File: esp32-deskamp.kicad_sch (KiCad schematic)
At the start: 3 parts, among them K1 TQ2-12V, U1 ESP32 D1 Mini, U2 TSR 1-2433

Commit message: Rebuild chunk of schematic
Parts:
- added D1, D2, D3, D4: 1N4004, Diode_THT:D_DO-41_SOD81_P10.16mm_Horizontal, symbol Diode:1N4004
- added J1: INPUT 00, symbol Connector:Conn_01x04_Pin
- added J10: SLEEP, symbol Connector:Conn_01x02_Pin
- added J2: INPUT 01, symbol Connector:Conn_01x04_Pin
- added J3: PRE OUT, symbol Connector:Conn_01x04_Pin
- added J4: LFE OUT, symbol Connector:Conn_01x02_Pin
- added J5: 12V IN, symbol Connector:Conn_01x02_Pin
- added J6, J7: JUMPER, symbol Connector:Conn_01x03_Pin
- added J8: INPUT SELECT, symbol Connector:Conn_01x04_Pin
- added J9: MUTE, symbol Connector:Conn_01x02_Pin
- added K2: INPUT 01, RELAY_TQ2_PAN, symbol panasonic-tq2:TQ2-12V
- added K3: AMP MUTE, RELAY_TQ2_PAN, symbol panasonic-tq2:TQ2-12V
- added K4: AMP SLEEP, RELAY_TQ2_PAN, symbol panasonic-tq2:TQ2-12V
- added Q1, Q2, Q3, Q4: 2N3904, Package_TO_SOT_THT:TO-92_Inline, symbol Transistor_BJT:2N3904
- added R1, R2, R5, R6: 1K6, symbol Device:R
- added R3, R4, R7, R8, R9: 10K, symbol Device:R
- added RV1: RK27112MC, Potentiometer_THT:Potentiometer_Alps_RK27112MC, symbol custom:RK27112MC
- added U3: L9110, symbol L9110:L9110
- K1: value TQ2-12V -> INPUT 00
- U1: value ESP32 D1 Mini -> ESP32 D1 MINI
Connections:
- net +12V: now also K1.1, D1.1 (K), D2.1 (K), D3.1 (K), D4.1 (K), J5.1 (Pin_1), K2.1, K3.1, K4.1
- net +3V3: now also U1.16 (3V3), R7.1, R8.1, R9.1
- net at K1.10: now also D1.2 (A), Q1.3 (C)
- net at K1.3: now also J1.1 (Pin_1)
- net PRE_RIGHT: now reaches K1.4
- net PRE_RIGHT: now also K2.4, RV1.4
- net PRE_LEFT: now reaches K1.7
- net PRE_LEFT: now also K2.7, RV1.1
- net at K1.8: now also J1.2 (Pin_2)
- net GNDD renamed GNDS
- net GNDS: now also J5.2 (Pin_2), J8.1 (Pin_1), Q1.1 (E), Q2.1 (E), Q3.1 (E), Q4.1 (E)
- new net: Q1.2 (B), R1.1
- new net: Q4.2 (B), R6.1
- new net: D4.2 (A), K4.10, Q4.3 (C)
- new net: D3.2 (A), K3.10, Q3.3 (C)
- new net: J6.3 (Pin_3), J9.1 (Pin_1)
- new net: J6.2 (Pin_2), J9.2 (Pin_2), K3.4
- new net: J2.1 (Pin_1), K2.3
- new net: J2.2 (Pin_2), K2.8
- new net: D2.2 (A), K2.10, Q2.3 (C)
- new net: Q3.2 (B), R5.1
- new net: J10.1 (Pin_1), J7.3 (Pin_3)
- new net: J10.2 (Pin_2), J7.2 (Pin_2), K4.4
- new net: J4.2 (Pin_2), R3.1, R4.1
- new net: J3.3 (Pin_3), R3.2, RV1.5
- new net: J3.4 (Pin_4), R4.2, RV1.2
- new net: Q2.2 (B), R2.1
- new net: J7.1 (Pin_1), K4.3
- new net: J6.1 (Pin_1), K3.3
- new net GNDA: J1.3 (Pin_3), J1.4 (Pin_4), J2.3 (Pin_3), J2.4 (Pin_4), J3.1 (Pin_1), J3.2 (Pin_2), J4.1 (Pin_1), RV1.3, RV1.6
- new net Input0: R1.2
- new net Input1: R2.2
- new net Mute: R5.2
- new net Select0: J8.4 (Pin_4), R9.2
- new net Select1: J8.3 (Pin_3), R8.2
- new net Select3: J8.2 (Pin_2), R7.2
- new net Sleep: R6.2
- no-connect marks 0 -> 20
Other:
- note added: "INPUT SELECT"
- note added: "OUTPUT STAGE"
- note added: "POWER"
- note added: "TA2024 USES SWITCH LOGIC TO ACTIVATE MUTE/SLEEP. JUMPER 1/2 FOR DIRECT, 2/3 VIA JST."
- moved on the sheet: K1, U1, U2

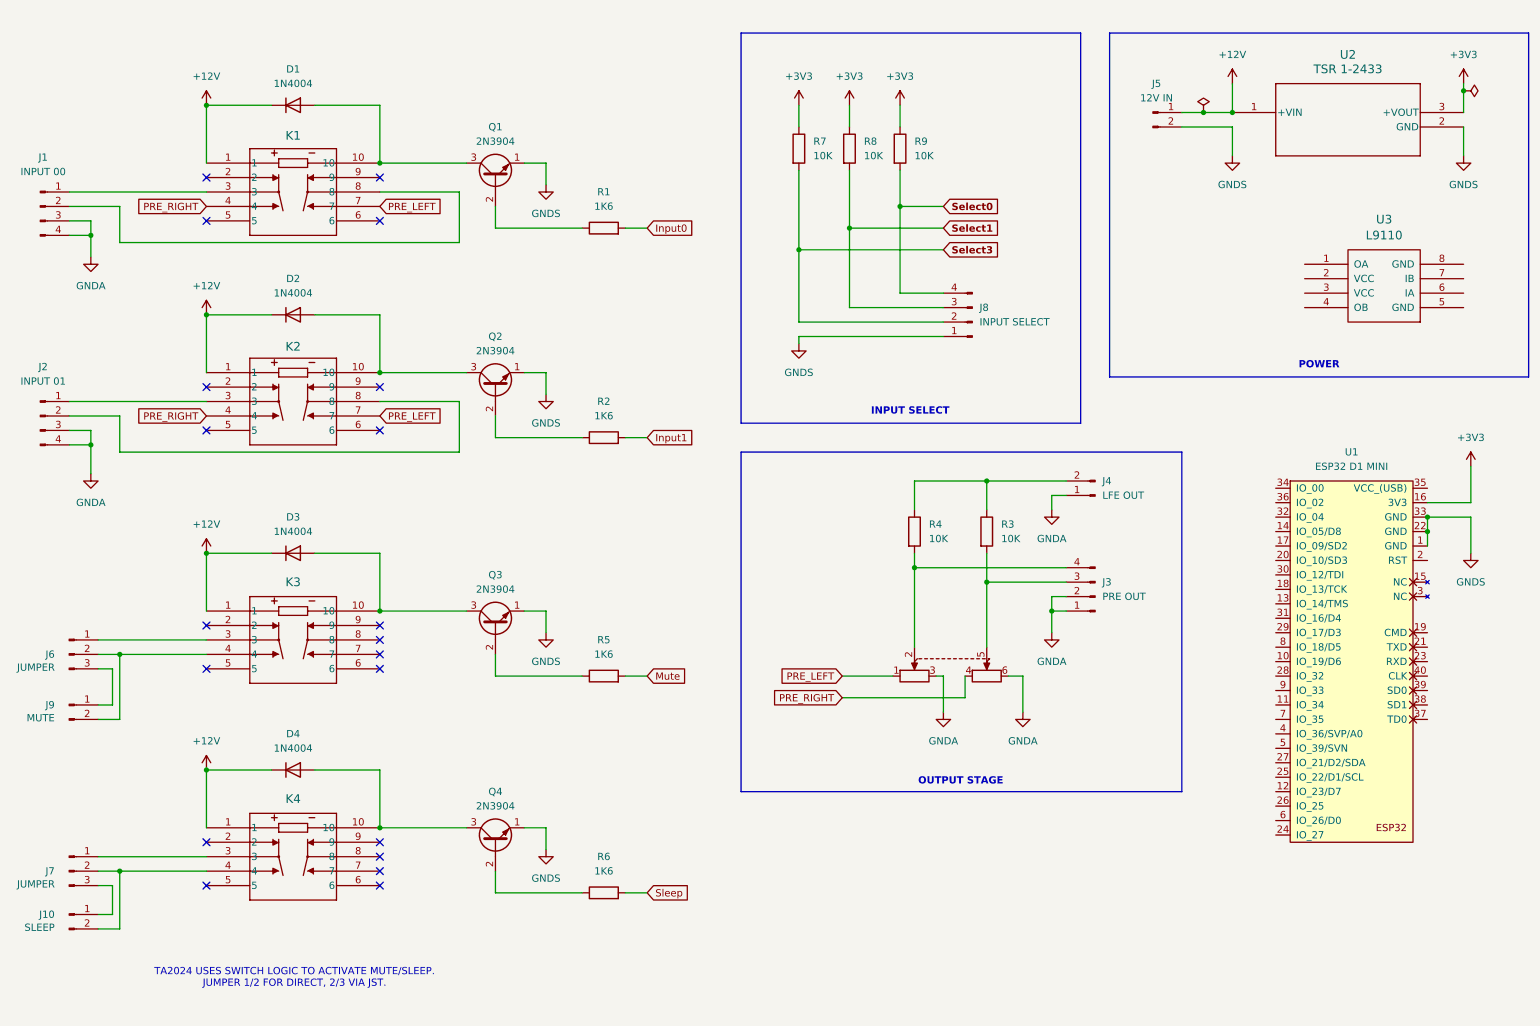
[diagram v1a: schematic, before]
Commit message: Start routing, remove duplicate project
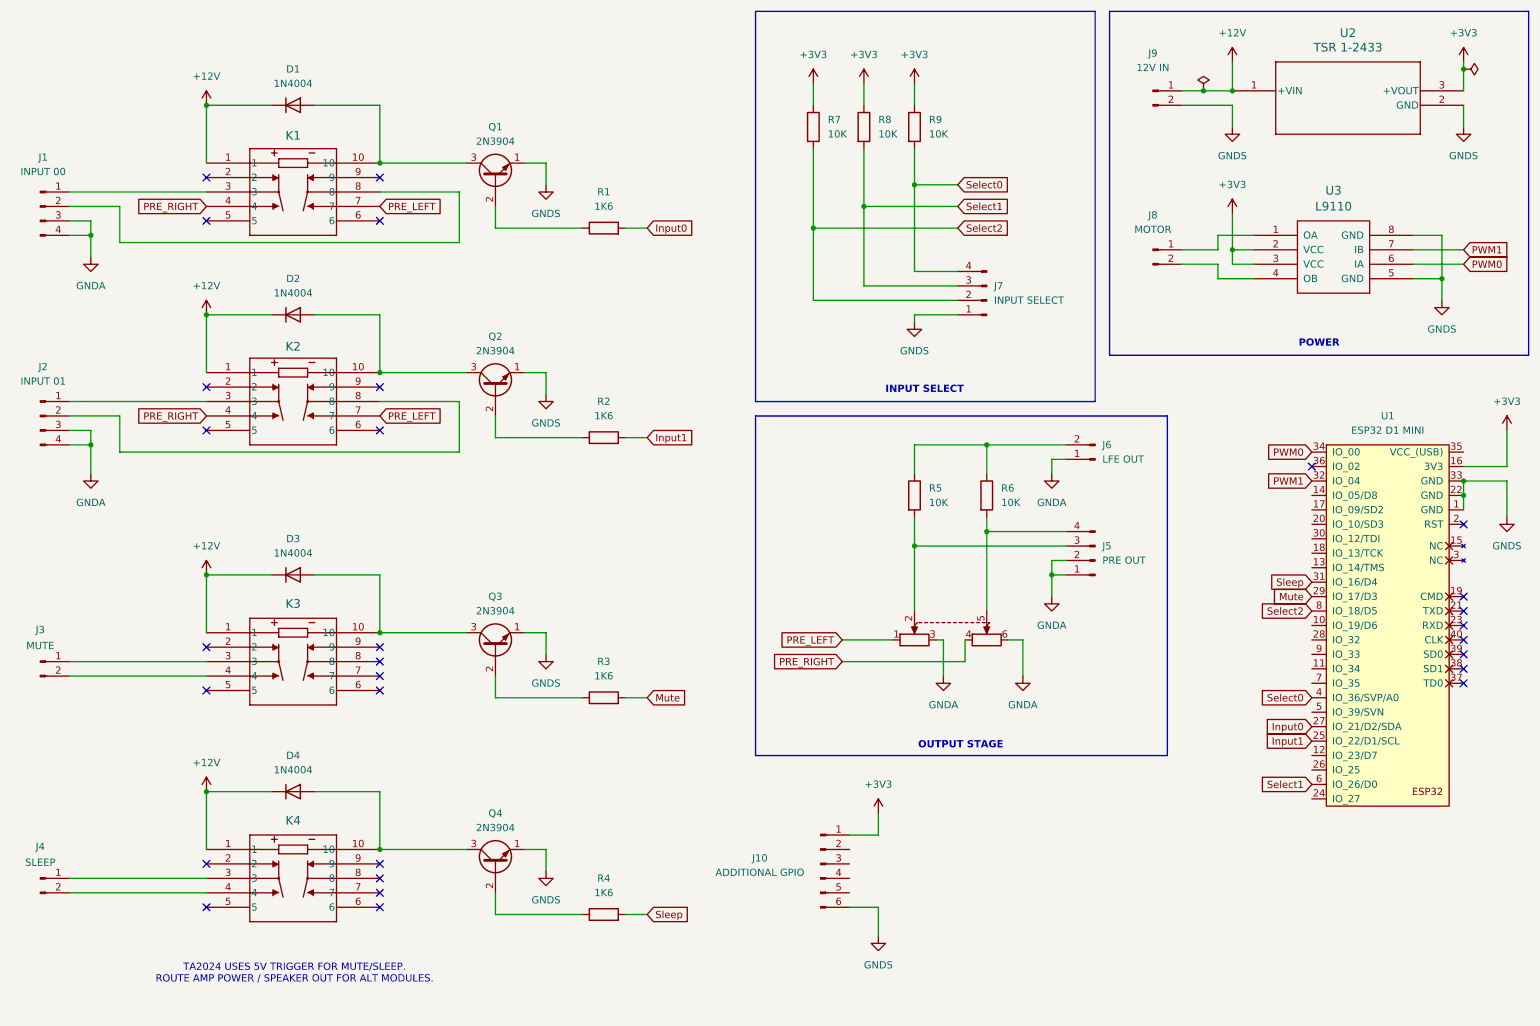
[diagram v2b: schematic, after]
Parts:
- removed J10: SLEEP, symbol Connector:Conn_01x02_Pin
- removed J7: JUMPER, symbol Connector:Conn_01x03_Pin
- removed J9: MUTE, symbol Connector:Conn_01x02_Pin
- added J10: ADDITIONAL GPIO, Connector_PinHeader_2.54mm:PinHeader_1x06_P2.54mm_Vertical, symbol Connector:Conn_01x06_Pin
- added J4: SLEEP, TerminalBlock:TerminalBlock_MaiXu_MX126-5.0-02P_1x02_P5.00mm, symbol Connector:Conn_01x02_Pin
- added J8: MOTOR, Connector_JST:JST_XH_B2B-XH-A_1x02_P2.50mm_Vertical, symbol Connector:Conn_01x02_Pin
- D1, D2, D3, D4: footprint Diode_THT:D_DO-41_SOD81_P10.16mm_Horizontal -> Diode_THT:D_DO-35_SOD27_P7.62mm_Horizontal
- J1, J2: footprint (none) -> Connector_JST:JST_XH_B4B-XH-A_1x04_P2.50mm_Vertical
- J3: renamed from J6; value JUMPER -> MUTE; footprint (none) -> TerminalBlock:TerminalBlock_MaiXu_MX126-5.0-02P_1x02_P5.00mm; symbol Connector:Conn_01x03_Pin -> Connector:Conn_01x02_Pin
- J5: renamed from J3; footprint (none) -> Connector_JST:JST_XH_B4B-XH-A_1x04_P2.50mm_Vertical
- J6: renamed from J4; footprint (none) -> Connector_JST:JST_XH_B2B-XH-A_1x02_P2.50mm_Vertical
- J7: renamed from J8; footprint (none) -> Connector_JST:JST_XH_B4B-XH-A_1x04_P2.50mm_Vertical
- J9: renamed from J5; footprint (none) -> Connector_JST:JST_XH_B2B-XH-A_1x02_P2.50mm_Vertical
- K1, K2, K3, K4: footprint RELAY_TQ2_PAN -> TQ2:RELAY_TQ2_PAN
- R1, R2, R7, R8, R9: footprint (none) -> Resistor_SMD:R_0805_2012Metric_Pad1.20x1.40mm_HandSolder
- R3: renamed from R5; footprint (none) -> Resistor_SMD:R_0805_2012Metric_Pad1.20x1.40mm_HandSolder
- R4: renamed from R6; footprint (none) -> Resistor_SMD:R_0805_2012Metric_Pad1.20x1.40mm_HandSolder
- R5: renamed from R4; footprint (none) -> Resistor_THT:R_Axial_Power_L38.0mm_W9.0mm_P40.64mm
- R6: renamed from R3; footprint (none) -> Resistor_THT:R_Axial_Power_L38.0mm_W9.0mm_P40.64mm
- U1: footprint esp32-wemos-d1-mini:esp32-wemos-d1-mini -> ESP32 D1 Mini:esp32-wemos-d1-mini
- U2: footprint TSR1-SINGLE_TRP -> TSR-2433:TSR1-SINGLE_TRP
- U3: footprint (none) -> Package_DIP:DIP-8_W7.62mm
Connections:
- net Select3 is gone; now on net Select2: J7.2 (Pin_2), R7.2
- net +3V3: now also U3.2 (VCC), U3.3 (VCC), J10.1 (Pin_1)
- net GNDS: now also U3.5 (GND), U3.8 (GND), J10.6 (Pin_6)
- net Input0: now also U1.27 (IO_21/D2/SDA)
- net Input1: now also U1.25 (IO_22/D1/SCL)
- net Mute: now also U1.29 (IO_17/D3)
- net Select0: now also U1.4 (IO_36/SVP/A0)
- net Select1: now also U1.6 (IO_26/D0)
- net Sleep: now also U1.31 (IO_16/D4)
- net at K4.4: now also J4.2 (Pin_2)
- net at R6.2, RV1.5: now also J5.4 (Pin_4); no longer J5.3 (Pin_3)
- net at R5.2, RV1.2: now also J5.3 (Pin_3); no longer J5.4 (Pin_4)
- net at K4.3: now also J4.1 (Pin_1)
- net at U3.1 (OA): now also J8.1 (Pin_1)
- net at U3.4 (OB): now also J8.2 (Pin_2)
- net PWM0: now reaches U3.6 (IA)
- net PWM0: now also U1.34 (IO_00)
- net PWM1: now reaches U3.7 (IB)
- net PWM1: now also U1.32 (IO_04)
- net Select2: now reaches U1.8 (IO_18/D5)
- no-connect marks 20 -> 29
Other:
- note added: "TA2024 USES 5V TRIGGER FOR MUTE/SLEEP. ROUTE AMP POWER / SPEAKER OUT FOR ALT MODULES."
- note removed: "TA2024 USES SWITCH LOGIC TO ACTIVATE MUTE/SLEEP. JUMPER 1/2 FOR DIRECT, 2/3 VIA JST."
- moved on the sheet: D3, D4, J5, J6, J7, J9, K3, K4, Q3, Q4, R3, R4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

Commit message: Locked in routing for relays
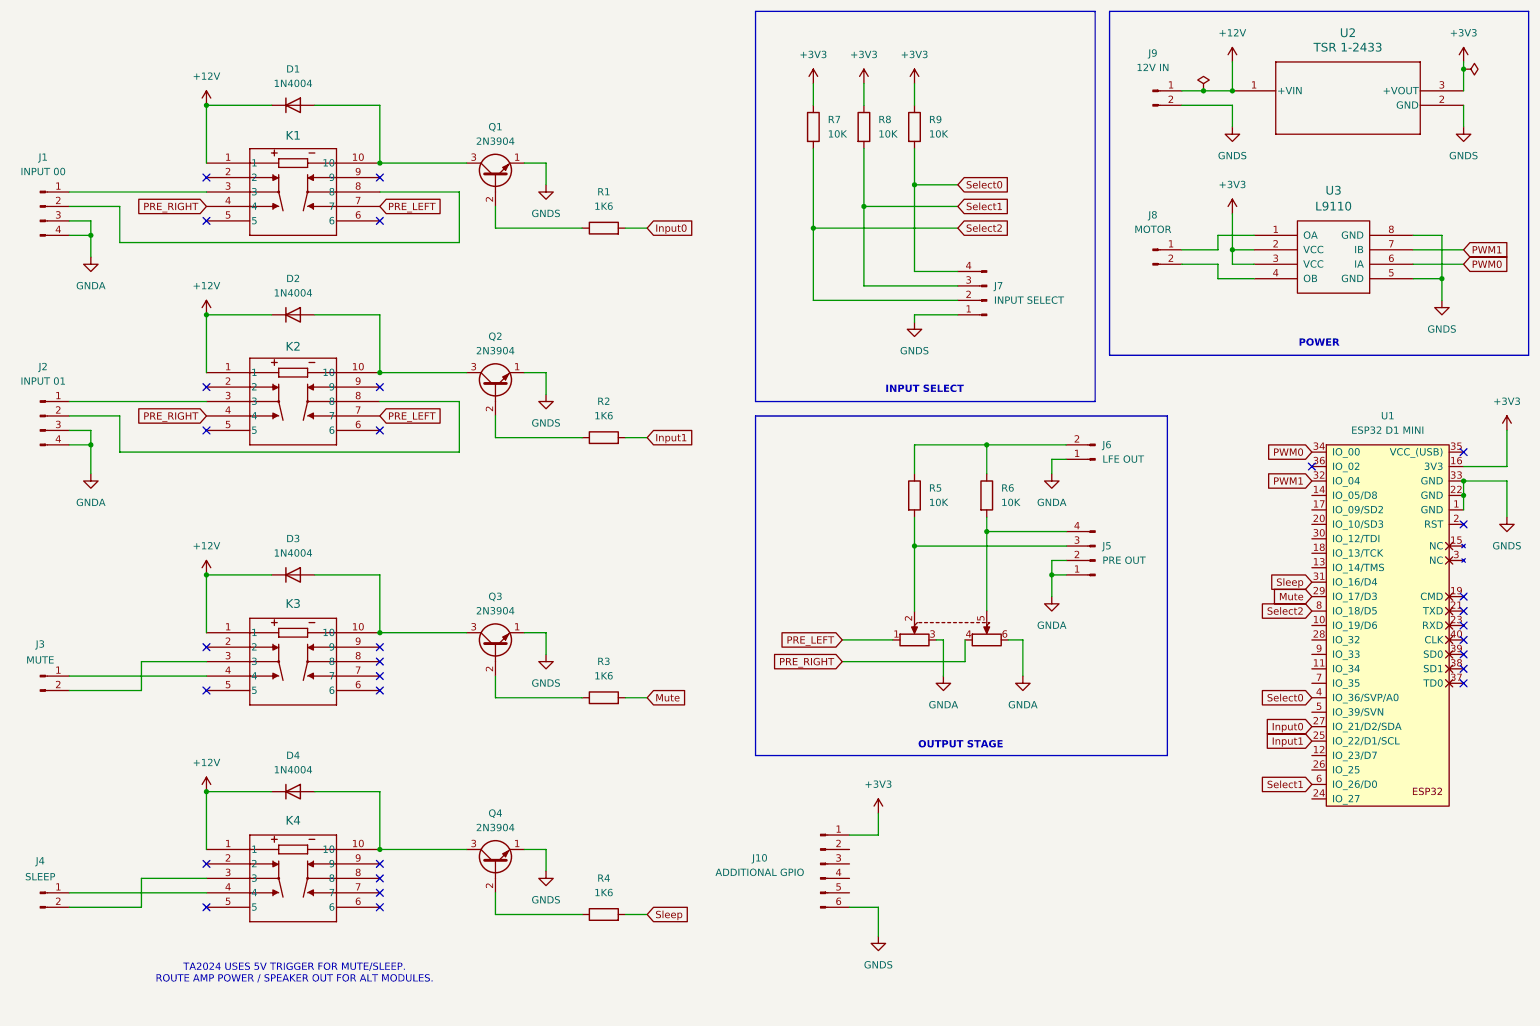
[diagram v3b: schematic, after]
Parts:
- J3, J4: footprint TerminalBlock:TerminalBlock_MaiXu_MX126-5.0-02P_1x02_P5.00mm -> Connector_JST:JST_XH_B2B-XH-A_1x02_P2.50mm_Vertical
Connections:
- net at J4.1 (Pin_1): now also K4.4; no longer K4.3
- net at J4.2 (Pin_2): now also K4.3; no longer K4.4
- net at K3.3: now also J3.2 (Pin_2); no longer J3.1 (Pin_1)
- net at K3.4: now also J3.1 (Pin_1); no longer J3.2 (Pin_2)
- no-connect marks 29 -> 30
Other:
- moved on the sheet: J3, J4
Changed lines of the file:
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@@
 	)
 	(no_connect
+		(at 267.97 92.71)
+	)
+	(no_connect
 		(at 77.47 44.45)
 	)
@@
 	(wire
 		(pts
+			(xy 35.56 172.72) (xy 22.86 172.72)
+		)
+		(stroke
+			(width 0)
+			(type default)
+		)
+	)
+	(wire
+		(pts
+			(xy 46.99 167.64) (xy 35.56 167.64)
+		)
+		(stroke
+			(width 0)
+			(type default)
+		)
+	)
+	(wire
+		(pts
 			(xy 184.15 104.14) (xy 184.15 106.68)
 		)
@@
 	(wire
 		(pts
-			(xy 22.86 132.08) (xy 46.99 132.08)
+			(xy 158.75 129.54) (xy 180.34 129.54)
 		)
 		(stroke
@@
 	(wire
 		(pts
-			(xy 158.75 129.54) (xy 180.34 129.54)
+			(xy 22.86 54.61) (xy 26.67 54.61)
 		)
 		(stroke
@@
 	(wire
 		(pts
-			(xy 22.86 54.61) (xy 26.67 54.61)
+			(xy 171.45 104.14) (xy 171.45 109.22)
 		)
 		(stroke
@@
 	(wire
 		(pts
-			(xy 171.45 104.14) (xy 171.45 109.22)
+			(xy 190.5 125.73) (xy 190.5 132.08)
 		)
 		(stroke
@@
 	(wire
 		(pts
-			(xy 190.5 125.73) (xy 190.5 132.08)
+			(xy 22.86 134.62) (xy 35.56 134.62)
 		)
 		(stroke
@@
 	(wire
 		(pts
-			(xy 22.86 167.64) (xy 46.99 167.64)
+			(xy 106.68 41.91) (xy 106.68 45.72)
 		)
 		(stroke
@@
 	(wire
 		(pts
-			(xy 106.68 41.91) (xy 106.68 45.72)
+			(xy 35.56 129.54) (xy 46.99 129.54)
 		)
 		(stroke
@@
 	(wire
 		(pts
-			(xy 22.86 170.18) (xy 46.99 170.18)
+			(xy 22.86 132.08) (xy 46.99 132.08)
 		)
 		(stroke
@@
 	(wire
 		(pts
+			(xy 35.56 167.64) (xy 35.56 172.72)
+		)
+		(stroke
+			(width 0)
+			(type default)
+		)
+	)
+	(wire
+		(pts
 			(xy 224.79 62.23) (xy 231.14 62.23)
 		)
@@
 	(wire
 		(pts
+			(xy 46.99 170.18) (xy 22.86 170.18)
+		)
+		(stroke
+			(width 0)
+			(type default)
+		)
+	)
+	(wire
+		(pts
 			(xy 224.79 54.61) (xy 231.14 54.61)
 		)
@@
 	(wire
 		(pts
-			(xy 120.65 90.17) (xy 124.46 90.17)
+			(xy 35.56 134.62) (xy 35.56 129.54)
 		)
 		(stroke
@@
 	(wire
 		(pts
-			(xy 184.15 106.68) (xy 184.15 120.65)
+			(xy 120.65 90.17) (xy 124.46 90.17)
 		)
 		(stroke
@@
 	(wire
 		(pts
-			(xy 26.67 52.07) (xy 26.67 54.61)
+			(xy 184.15 106.68) (xy 184.15 120.65)
 		)
 		(stroke
@@
 	(wire
 		(pts
-			(xy 264.16 62.23) (xy 264.16 66.04)
+			(xy 26.67 52.07) (xy 26.67 54.61)
 		)
 		(stroke
@@
 	(wire
 		(pts
-			(xy 22.86 129.54) (xy 46.99 129.54)
+			(xy 264.16 62.23) (xy 264.16 66.04)
 		)
 		(stroke
@@
 	(symbol
 		(lib_id "Connector:Conn_01x02_Pin")
-		(at 17.78 167.64 0)
+		(at 17.78 170.18 0)
 		(unit 1)
 		(exclude_from_sim no)
@@
 		(dnp no)
 		(property "Reference" "J4"
-			(at 17.78 162.052 0)
+			(at 17.78 164.592 0)
 			(effects
 				(font
@@
 		)
 		(property "Value" "SLEEP"
-			(at 17.78 164.846 0)
+			(at 17.78 167.386 0)
 			(effects
 				(font
@@
 			)
 		)
-		(property "Footprint" "TerminalBlock:TerminalBlock_MaiXu_MX126-5.0-02P_1x02_P5.00mm"
-			(at 17.78 167.64 0)
+		(property "Footprint" "Connector_JST:JST_XH_B2B-XH-A_1x02_P2.50mm_Vertical"
+			(at 17.78 170.18 0)
 			(effects
 				(font
@@
 		)
 		(property "Datasheet" "~"
-			(at 17.78 167.64 0)
+			(at 17.78 170.18 0)
 			(effects
 				(font
@@
 		)
 		(property "Description" "Generic connector, single row, 01x02, script generated"
-			(at 17.78 167.64 0)
+			(at 17.78 170.18 0)
 			(effects
 				(font
@@
 	(symbol
 		(lib_id "Connector:Conn_01x02_Pin")
-		(at 17.78 129.54 0)
+		(at 17.78 132.08 0)
 		(unit 1)
 		(exclude_from_sim no)
@@
 		(dnp no)
 		(property "Reference" "J3"
-			(at 17.78 123.952 0)
+			(at 17.78 126.492 0)
 			(effects
 				(font
@@
 		)
 		(property "Value" "MUTE"
-			(at 17.78 126.746 0)
+			(at 17.78 129.286 0)
 			(effects
 				(font
@@
 			)
 		)
-		(property "Footprint" "TerminalBlock:TerminalBlock_MaiXu_MX126-5.0-02P_1x02_P5.00mm"
-			(at 17.78 129.54 0)
+		(property "Footprint" "Connector_JST:JST_XH_B2B-XH-A_1x02_P2.50mm_Vertical"
+			(at 17.78 132.08 0)
 			(effects
 				(font
@@
 		)
 		(property "Datasheet" "~"
-			(at 17.78 129.54 0)
+			(at 17.78 132.08 0)
 			(effects
 				(font
@@
 		)
 		(property "Description" "Generic connector, single row, 01x02, script generated"
-			(at 17.78 129.54 0)
+			(at 17.78 132.08 0)
 			(effects
 				(font

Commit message: Milestone, may tweak layout
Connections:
- net PRE_LEFT: now also RV1.4; no longer RV1.1
- net PRE_RIGHT: now also RV1.1; no longer RV1.4

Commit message: V3
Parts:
- removed Q1, Q2, Q3, Q4: 2N3904, Package_TO_SOT_THT:TO-92_Inline, symbol Transistor_BJT:2N3904
- removed R1, R2, R3, R4: 1K6, Resistor_SMD:R_0805_2012Metric_Pad1.20x1.40mm_HandSolder, symbol Device:R
- added C1: 10uF, Capacitor_THT:DX_5R5VxxxxU_D11.5mm_P5.00mm, symbol Device:C_Polarized
- added U4: ULN2003A, Package_SO:SSOP-16_4.4x5.2mm_P0.65mm, symbol Transistor_Array:ULN2003A
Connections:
- net +12V: now also C1.1, U4.9 (COM)
- net GNDA: now also J5.3 (Pin_3), J5.4 (Pin_4), J6.2 (Pin_2); no longer J5.1 (Pin_1), J5.2 (Pin_2), J6.1 (Pin_1)
- net GNDS: now also C1.2, U4.8 (GND)
- net Input0: now also U4.6 (I6)
- net Input1: now also U4.7 (I7)
- net Mute: now also U4.4 (I4)
- net Sleep: now also U4.5 (I5)
- net Relay0: now reaches D1.2 (A), K1.10
- net Relay0: now also U4.11 (O6)
- net Relay3: now reaches D4.2 (A), K4.10
- net Relay3: now also U4.12 (O5)
- net Relay2: now reaches D3.2 (A), K3.10
- net Relay2: now also U4.13 (O4)
- net Relay1: now reaches D2.2 (A), K2.10
- net Relay1: now also U4.10 (O7)
- net at R5.1, R6.1: now also J6.1 (Pin_1); no longer J6.2 (Pin_2)
- net at R6.2, RV1.5: now also J5.1 (Pin_1); no longer J5.4 (Pin_4)
- net at J8.1 (Pin_1): now also U3.4 (OB); no longer U3.1 (OA)
- net at J8.2 (Pin_2): now also U3.1 (OA); no longer U3.4 (OB)
- net at R5.2, RV1.2: now also J5.2 (Pin_2); no longer J5.3 (Pin_3)
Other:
- moved on the sheet: D3, D4, J3, J4, K3, K4
